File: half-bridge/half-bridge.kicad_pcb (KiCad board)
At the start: 4 copper layers, 56.6 x 37.1 mm, 50 parts, among them J1 Conn_01x11_Pin, J2 Conn_01x11_Pin, J3 Conn_01x04_Pin, J4 Conn_01x04_Pin, J5 Conn_01x11_Pin, J6 Conn_01x11_Pin, J7 Conn_01x11_Pin, J8 Conn_01x11_Pin, Q1 GAN7R0-150LBE, Q2 GAN7R0-150LBE, U1 LMG1210

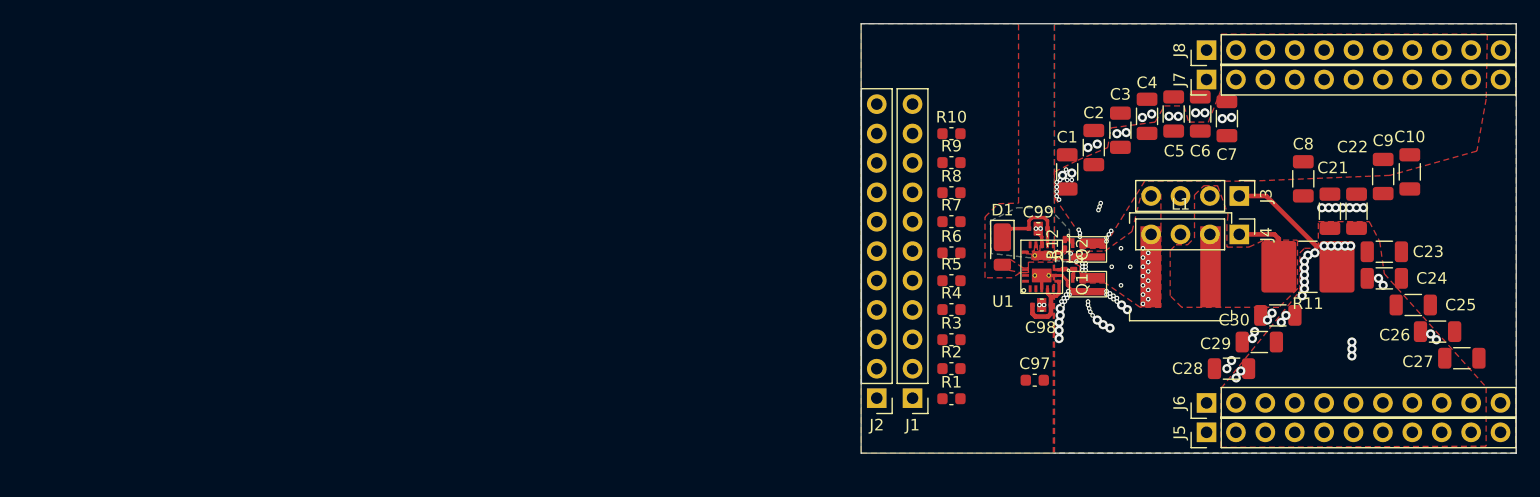
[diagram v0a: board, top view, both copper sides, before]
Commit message: More work mainly on layout
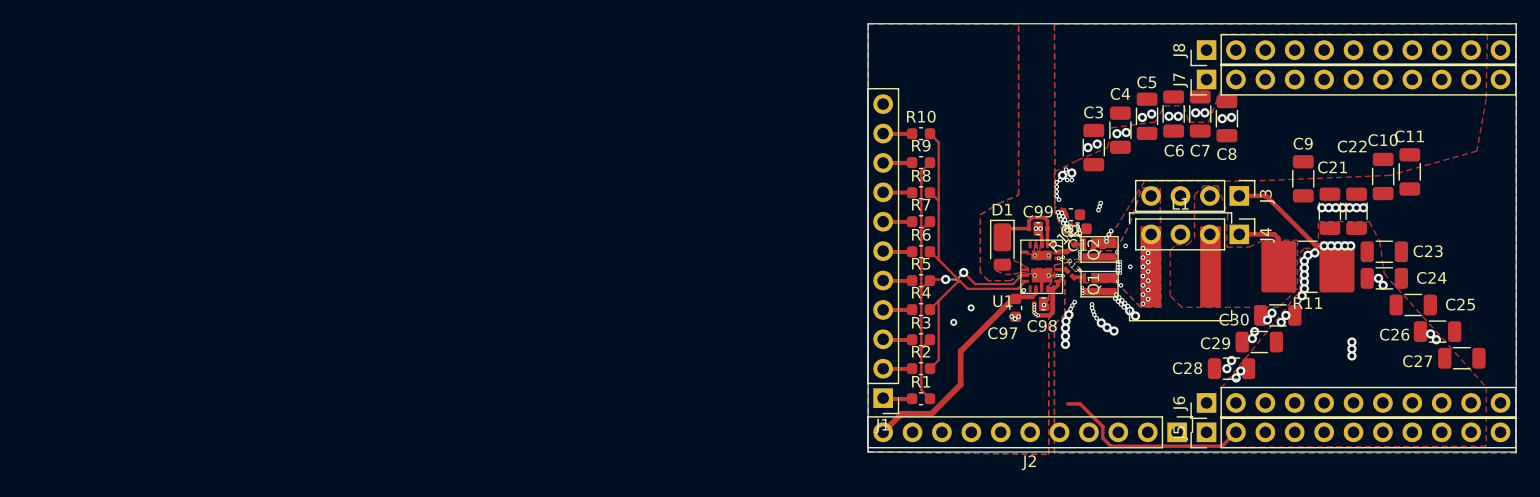
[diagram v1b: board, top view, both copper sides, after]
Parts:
- added C2: C_Small, Capacitor_SMD:C_0603_1608Metric, F.Cu at (130.5, 95.5)
- C1: value C -> C_Small; footprint Capacitor_SMD:C_1206_3216Metric -> Capacitor_SMD:C_0603_1608Metric
- moved J2 26.1 mm to (139.7, 114.3), turned to -90 degrees
- moved C97 6.46 mm to (125.8, 103.5), turned to -90 degrees
- moved C1 5.01 mm to (131.1, 96.7), turned to 180 degrees
- moved R6 2.63 mm to (117.6, 98.7)
- moved R1 2.62 mm to (117.6, 111.4)
- moved R10 2.62 mm to (117.6, 88.5)
- moved R2 2.62 mm to (117.6, 108.8)
- moved R3 2.62 mm to (117.6, 106.3)
- moved R4 2.62 mm to (117.6, 103.7)
- moved R5 2.62 mm to (117.6, 101.2)
- moved R7 2.62 mm to (117.6, 96.1)
- moved R8 2.62 mm to (117.6, 93.6)
- moved R9 2.62 mm to (117.6, 91.0)
- moved J1 2.54 mm to (114.3, 111.3)
- moved Q1 1.00 mm to (133.0, 101.5)
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- renumbered C9 to C10, C10 to C11, C2 to C3, C3 to C4, C4 to C5, C5 to C6, C6 to C7, C7 to C8, C8 to C9
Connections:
- U1 pad 5: unconnected-(U1-DHL-Pad5) -> +5V
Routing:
- net Net-(U1-EN/HI): track 0.00 -> 33.4 mm, vias 0 -> 2
- net Net-(U1-PWM/LO): track 0.00 -> 31.9 mm
- net 6-18V: track 0.00 -> 20.3 mm
- net Net-(J3-Pin_1): track 11.4 -> 28.6 mm
- net Net-(J1-Pin_8): track 0.00 -> 5.11 mm
- net Net-(J1-Pin_9): track 0.00 -> 5.11 mm
- net Net-(J1-Pin_4): track 0.00 -> 5.11 mm
- net Net-(J1-Pin_7): track 0.00 -> 5.09 mm
- net Net-(J1-Pin_2): track 0.00 -> 5.09 mm
- net Net-(J1-Pin_5): track 0.00 -> 5.08 mm
- net Net-(J1-Pin_10): track 0.00 -> 5.08 mm
- net Net-(J1-Pin_3): track 0.00 -> 5.07 mm
- net Net-(J1-Pin_6): track 0.00 -> 5.05 mm
- net Net-(J1-Pin_1): track 0.00 -> 5.05 mm
- net GNDPWR: track 3.84 -> 2.62 mm, vias 50 -> 65
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- added copper zone on In2.Cu, net +5V
- added copper zone on B.Cu, net Earth
- added copper zone on In1.Cu, net Earth
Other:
- board size 56.6 x 37.1 mm -> 56 x 37 mm

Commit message: Some changes
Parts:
- added C96: 10uF, Capacitor_SMD:C_0603_1608Metric, F.Cu at (127.7, 105.5)
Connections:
- net Net-(J3-Pin_1) renamed POWER_LOW
- net Vbus renamed POWER_HIGH
- J2 pad 1: unconnected-(J2-Pin_1-Pad1) -> Net-(J2-Pin_1)
- J2 pad 2: unconnected-(J2-Pin_2-Pad2) -> Net-(J2-Pin_2)
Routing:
- net Switch_node: vias 36 -> 40
- net Earth: vias 6 -> 15
- net +5V: vias 6 -> 5

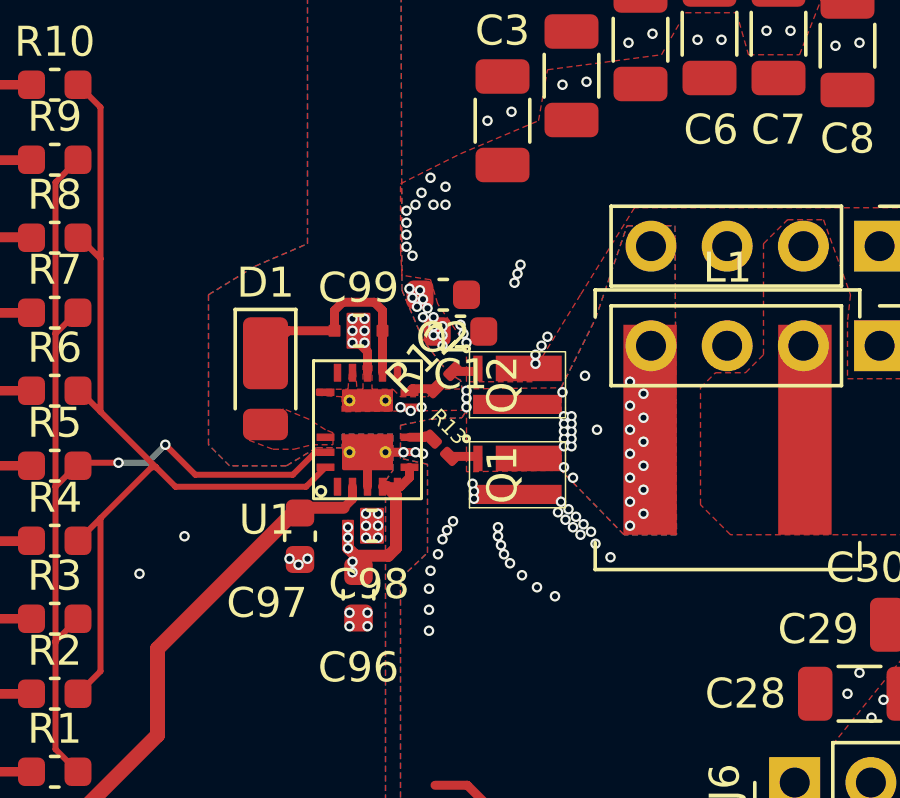
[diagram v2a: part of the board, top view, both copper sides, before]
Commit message: Add drc rules and fix some errors
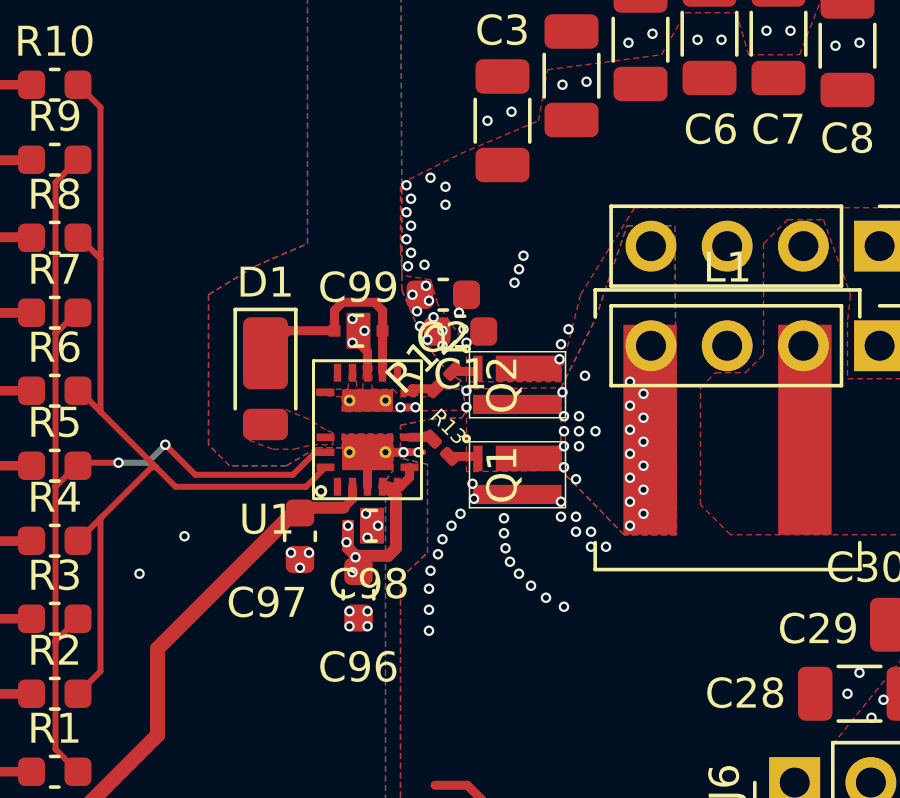
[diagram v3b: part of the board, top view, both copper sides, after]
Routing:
- net Switch_node: vias 40 -> 31
- net POWER_HIGH: vias 27 -> 26
- net GNDPWR: vias 65 -> 55
- net Earth: vias 15 -> 12
- net +5V: vias 5 -> 4

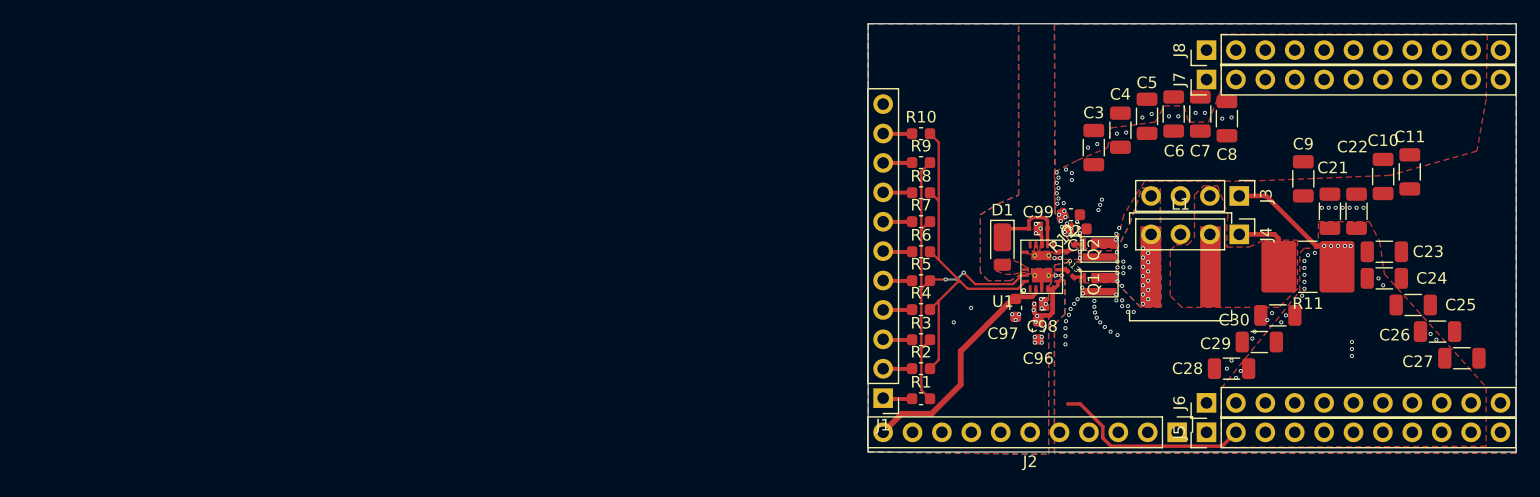
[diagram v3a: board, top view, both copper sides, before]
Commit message: Start adding inductor current sense, adjust some vias and add input filtering
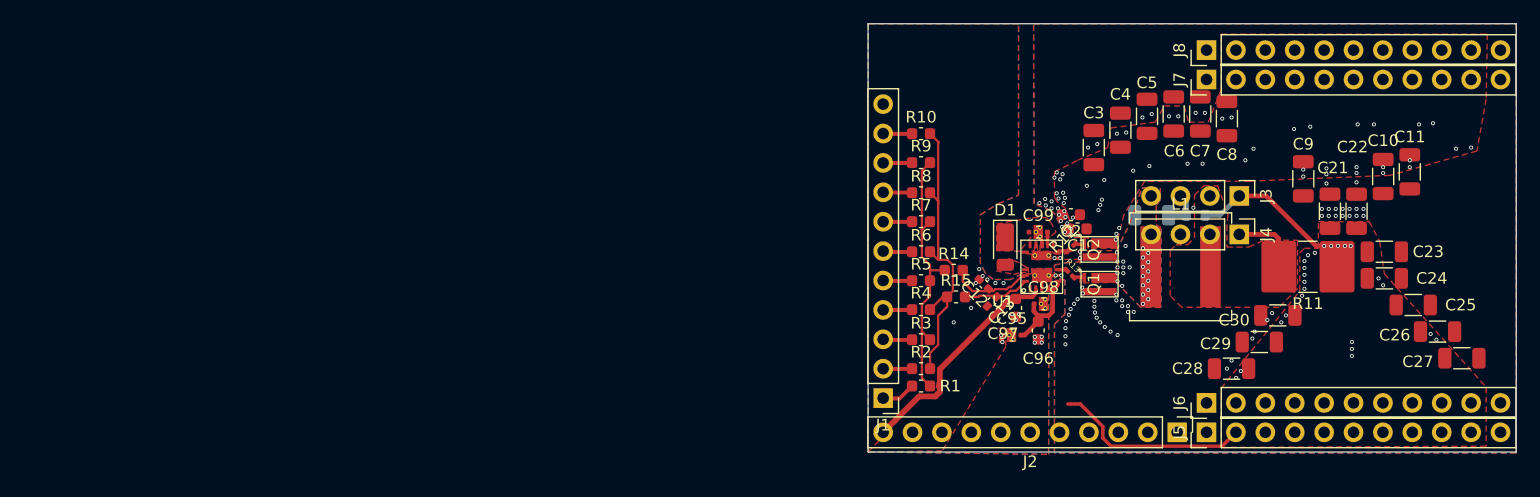
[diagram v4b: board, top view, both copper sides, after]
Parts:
- added C12: ?pF, Capacitor_SMD:C_0402_1005Metric_Pad0.74x0.62mm_HandSolder, F.Cu at (123.0, 101.5)
- added C13: ?pF, Capacitor_SMD:C_0402_1005Metric_Pad0.74x0.62mm_HandSolder, F.Cu at (123.7, 103.0)
- added C14: C_Small, Resistor_SMD:R_0603_1608Metric, B.Cu at (141.3, 95.5)
- added C95: YFF18PW0J474M, Library:C_0603_1608Metric_Feedthrough_W_Vias, F.Cu at (125.4, 105.9)
- added R14: 100R, Capacitor_SMD:C_0603_1608Metric, F.Cu at (120.4, 100.3)
- added R15: 100R, Capacitor_SMD:C_0603_1608Metric, F.Cu at (120.6, 102.6)
- added R16: R_Small, Resistor_SMD:R_1206_3216Metric, B.Cu at (137.5, 95.5)
- C98, C99: footprint Library:C_0603_1608Metric_Feedthrough -> Library:C_0603_1608Metric_Feedthrough_W_Vias
- moved R1 1.10 mm to (117.6, 110.3)
- moved C99 0.30 mm to (127.7, 97.0)
- moved D1 0.25 mm to (124.8, 98.3)
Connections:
- C96 pad 1: +5V -> Net-(U1-DHL)
- C98 pad 1: +5V -> Net-(U1-DHL)
- C98 pad 3: +5V -> Net-(U1-DHL)
- J3 pad 3: GNDPWR -> Current_sense
- R1 pad 2: Net-(U1-EN/HI) -> Net-(R1-Pad2)
- R10 pad 2: Net-(U1-PWM/LO) -> Net-(R10-Pad2)
- R2 pad 2: Net-(U1-PWM/LO) -> Net-(R10-Pad2)
- R3 pad 2: Net-(U1-EN/HI) -> Net-(R1-Pad2)
- R4 pad 2: Net-(U1-PWM/LO) -> Net-(R10-Pad2)
- R5 pad 2: Net-(U1-EN/HI) -> Net-(R1-Pad2)
- R6 pad 2: Net-(U1-PWM/LO) -> Net-(R10-Pad2)
- R7 pad 2: Net-(U1-EN/HI) -> Net-(R1-Pad2)
- R8 pad 2: Net-(U1-PWM/LO) -> Net-(R10-Pad2)
- R9 pad 2: Net-(U1-EN/HI) -> Net-(R1-Pad2)
- U1 pad 4: +5V -> Net-(U1-DHL)
- U1 pad 5: +5V -> Net-(U1-DHL)
- U1 pad 6: +5V -> Net-(U1-DHL)
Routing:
- net Net-(R10-Pad2): track 0.00 -> 26.8 mm
- net Net-(U1-EN/HI): track 33.4 -> 7.29 mm, vias 2 -> 0
- net Net-(U1-PWM/LO): track 31.9 -> 5.78 mm
- net Net-(R1-Pad2): track 0.00 -> 24.4 mm
- net Net-(U1-DHL): track 0.00 -> 8.01 mm
- net Net-(D1-K): track 7.19 -> 1.10 mm
- net +5V: track 6.10 -> 0.64 mm, vias 4 -> 2
- net POWER_LOW: track 28.6 -> 32.2 mm
- net Current_sense: track 0.00 -> 3.38 mm
- net GNDPWR: track 2.62 -> 0.45 mm, vias 55 -> 83
- net Net-(J1-Pin_1): track 5.05 -> 5.92 mm
- net 6-18V: track 20.3 -> 19.7 mm
- net Switch_node: track 1.26 -> 0.96 mm, vias 31 -> 28
- net POWER_HIGH: vias 26 -> 36
- net Earth: vias 12 -> 15
- added copper zone on F.Cu, net +5V
- added copper zone on F.Cu, net Net-(D1-K)
- added copper zone on In2.Cu, net POWER_LOW

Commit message: More work on current sense
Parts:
- removed R11: 10mOhm kanske?, Resistor_SMD:R_2816_7142Metric
- added NT2: NetTie_2, NetTie:NetTie-2_SMD_Pad0.5mm, F.Cu at (142.1, 96.2)
- moved C30 7.51 mm to (141.0, 105.5)
- moved C29 4.90 mm to (142.0, 107.5)
- moved C28 1.71 mm to (142.8, 109.4)
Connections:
- C14 pad 1: Current_sense -> Current_sense+
- J3 pad 2: Net-(J3-Pin_2) -> Current_sense+
- J3 pad 3: Current_sense -> GNDPWR
- J4 pad 1: Net-(J3-Pin_2) -> POWER_LOW
- J4 pad 2: Net-(J3-Pin_2) -> Current_sense-
- L1 pad 2: Net-(J3-Pin_2) -> POWER_LOW
- R16 pad 2: Current_sense -> Current_sense+
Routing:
- net Current_sense+: track 0.00 -> 30.7 mm, vias 0 -> 1
- net Current_sense-: track 0.00 -> 25.1 mm
- net POWER_LOW: track 32.2 -> 21.1 mm, vias 24 -> 55
- net Net-(J3-Pin_2): track 5.99 -> 0.00 mm
- net Current_sense: track 3.38 -> 0.00 mm
- net Switch_node: vias 28 -> 41
- net GNDPWR: vias 83 -> 160
- added copper zone on F.Cu, net Current_sense+
- removed copper zone on F.Cu, net Net-(J3-Pin_2)

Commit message: More work on layout
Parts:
- removed J3, J4: Conn_01x04_Pin, Connector_PinHeader_2.54mm:PinHeader_1x04_P2.54mm_Vertical
- added C31: C, Capacitor_SMD:C_1210_3225Metric, F.Cu at (157.6, 99.5)
- added C32: C, Capacitor_SMD:C_1210_3225Metric, F.Cu at (159.8, 102.7)
- added C33: C, Capacitor_SMD:C_1210_3225Metric, F.Cu at (165.6, 103.8)
- added C34: C, Capacitor_SMD:C_1210_3225Metric, F.Cu at (165.6, 107.0)
- moved C23 12.0 mm to (152.2, 109.4), turned to 180 degrees
- moved C25 10.3 mm to (150.0, 105.4), turned to 180 degrees
- moved C24 9.12 mm to (151.1, 107.4), turned to 180 degrees
- moved C14 8.68 mm to (140.2, 104.2)
- moved R16 8.25 mm to (137.3, 103.8), turned to -90 degrees
- moved NT2 7.17 mm to (140.8, 103.2)
- moved C27 4.20 mm to (160.1, 107.4)
- moved C26 3.18 mm to (159.0, 105.4)
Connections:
- C14 pad 2: POWER_LOW -> Current_sense-
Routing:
- net Current_sense+: track 30.7 -> 15.3 mm, vias 1 -> 3
- net Current_sense-: track 25.1 -> 17.6 mm, vias 0 -> 2
- net POWER_LOW: track 21.1 -> 17.1 mm, vias 55 -> 85
- net Earth: track 1.20 -> 4.37 mm, vias 15 -> 17
- net GNDPWR: track 0.45 -> 0.35 mm, vias 160 -> 240
- net POWER_HIGH: vias 36 -> 59
- removed copper zone on F.Cu, net Current_sense+

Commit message: More work on layout
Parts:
- added HS1: Heatsink_Pad, Library:Heatsink_SMD_Chamfered_5.2x5.2mm, F.Cu at (133.7, 94.4)
- added HS2: Heatsink_Pad, Library:Heatsink_SMD_Chamfered_5.2x5.2mm, F.Cu at (132.6, 105.4)
- added HS3: Heatsink_Pad, Library:Heatsink_SMD_Chamfered_5.2x5.2mm, B.Cu at (144.8, 100.0)
- C21, C22, C23, C24, C25, C26, C27, C28: value C -> 220nF
- C29, C30: value C -> 330nF; footprint Capacitor_SMD:C_1206_3216Metric -> Capacitor_SMD:C_1210_3225Metric
- C31, C32, C33, C34: value C -> 330nF
- moved C30 18.8 mm to (159.8, 105.5), turned to 0 degrees
- moved C27 18.1 mm to (142.0, 107.5), turned to 180 degrees
- moved C26 18.0 mm to (141.0, 105.5), turned to 180 degrees
- moved C29 17.9 mm to (159.8, 108.3), turned to 0 degrees
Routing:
- net POWER_LOW: vias 85 -> 105

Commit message: More work on layout for current signals
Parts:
- added J3: Conn_01x11_Pin, Connector_PinHeader_2.54mm:PinHeader_1x11_P2.54mm_Vertical, F.Cu at (139.7, 111.8)
- added R11: 0R, Capacitor_SMD:C_0402_1005Metric_Pad0.74x0.62mm_HandSolder, F.Cu at (128.7, 109.4)
- added R17: 0R, Capacitor_SMD:C_0402_1005Metric_Pad0.74x0.62mm_HandSolder, F.Cu at (127.8, 109.2)
- added R18: 0R, Capacitor_SMD:C_0402_1005Metric_Pad0.74x0.62mm_HandSolder, F.Cu at (126.8, 109.4)
- added R19: 0R, Capacitor_SMD:C_0402_1005Metric_Pad0.74x0.62mm_HandSolder, F.Cu at (125.8, 109.4)
- added R20: 0R, Capacitor_SMD:C_0402_1005Metric_Pad0.74x0.62mm_HandSolder, F.Cu at (124.8, 109.4)
- added R21: 0R, Capacitor_SMD:C_0402_1005Metric_Pad0.74x0.62mm_HandSolder, F.Cu at (123.9, 109.4)
- added R22: 0R, Capacitor_SMD:C_0402_1005Metric_Pad0.74x0.62mm_HandSolder, F.Cu at (123.0, 109.4)
- added R23: 0R, Capacitor_SMD:C_0402_1005Metric_Pad0.74x0.62mm_HandSolder, F.Cu at (122.0, 109.4)
- added R24: 0R, Capacitor_SMD:C_0402_1005Metric_Pad0.74x0.62mm_HandSolder, F.Cu at (121.0, 109.4)
- added R25: 0R, Capacitor_SMD:C_0402_1005Metric_Pad0.74x0.62mm_HandSolder, F.Cu at (120.1, 109.4)
- moved J1 2.13 mm to (114.3, 109.2)
- moved R4 2.10 mm to (117.6, 101.6)
- moved R5 2.10 mm to (117.6, 99.1)
- moved R6 2.10 mm to (117.6, 96.6)
- moved R1 2.10 mm to (117.6, 108.2)
- moved R10 2.10 mm to (117.6, 86.4)
- moved R2 2.10 mm to (117.6, 106.7)
- moved R3 2.10 mm to (117.6, 104.2)
- moved R7 2.10 mm to (117.6, 94.0)
- moved R8 2.10 mm to (117.6, 91.5)
- moved R9 2.10 mm to (117.6, 88.9)
- moved C33 0.75 mm to (166.3, 103.8)
- moved C34 0.75 mm to (166.3, 107.0)
- moved C29 0.15 mm to (159.7, 108.3)
- moved C30 0.15 mm to (159.7, 105.5)
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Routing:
- net Net-(J3-Pin_1): track 0.00 -> 12.1 mm, vias 0 -> 1
- net Current_sense-: track 17.6 -> 28.6 mm, vias 2 -> 3
- net Net-(J3-Pin_2): track 0.00 -> 10.8 mm, vias 0 -> 1
- net Net-(J3-Pin_3): track 0.00 -> 8.80 mm
- net Net-(J3-Pin_4): track 0.00 -> 7.45 mm, vias 0 -> 1
- net Net-(J3-Pin_5): track 0.00 -> 7.26 mm
- net +5V: track 0.64 -> 6.87 mm, vias 2 -> 7
- net Current_sense+: track 15.3 -> 21.1 mm, vias 3 -> 8
- net Net-(J3-Pin_6): track 0.00 -> 4.05 mm, vias 0 -> 1
- net Net-(J3-Pin_10): track 0.00 -> 4.01 mm
- net Net-(J1-Pin_1): track 5.92 -> 2.93 mm
- net Net-(J1-Pin_10): track 5.08 -> 2.52 mm
- net Net-(J1-Pin_9): track 5.11 -> 2.56 mm
- net Net-(J1-Pin_4): track 5.11 -> 2.56 mm
- net Net-(J1-Pin_8): track 5.11 -> 2.56 mm
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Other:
- board size 56 x 37 mm -> 56 x 36 mm
- board text added: "Fint namn här %%%date%% %%version%%"
- board text added: "TODO: What plane should we have here? None? ------------>"
